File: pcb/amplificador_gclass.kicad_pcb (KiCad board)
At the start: 2 copper layers, 72 parts, among them P1 CONN_01X02, P2 CONN_01X02, P3 CONN_01X02, P4 CONN_01X02, P5 BNC, P6 BNC, Q1 Q_PNP_EBC, Q10 Q_NPN_EBC, Q11 Q_PNP_EBC, Q12 Q_NPN_EBC, Q13 Q_PNP_EBC, Q14 Q_NPN_ECB, Q15 Q_PNP_EBC, Q16 Q_NPN_ECB, Q17 Q_NPN_ECB, Q18 Q_PNP_EBC, Q19 Q_NPN_ECB, Q2 Q_PNP_EBC, Q20 Q_PNP_EBC, Q21 Q_NPN_ECB, Q22 Q_PNP_EBC, Q23 Q_NPN_ECB, Q24 Q_NPN_ECB, Q25 Q_PNP_EBC, Q26 Q_PNP_EBC, Q3 Q_NPN_EBC, Q4 Q_PNP_EBC, Q5 Q_NPN_EBC, Q6 Q_PNP_EBC, Q7 Q_PNP_EBC, Q8 Q_PNP_EBC, Q9 Q_PNP_EBC

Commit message: Agrego algunos datasheets, el export kicad en pdf y sigo trabajando en el PCB
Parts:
- removed Q21: Q_NPN_ECB, Transistors_TO-220:TO-220_Bipolar-BCE_Vertical_LargePads
- removed Q22: Q_PNP_EBC, Transistors_TO-220:TO-220_Bipolar-BCE_Vertical_LargePads
- removed Q23, Q24: Q_NPN_ECB, Transistors_TO-220:TO-220_Bipolar-BCE_Horizontal
- removed Q25, Q26: Q_PNP_EBC, Transistors_TO-220:TO-220_Bipolar-BCE_Horizontal
- added C7: C, Capacitors_SMD:C_0603_HandSoldering, F.Cu at (178.1, 52.2)
- added P10: 2SC3281, Pin_Headers:Pin_Header_Straight_1x03, F.Cu at (138.3, 121.8)
- added P11: 2SC3281, Pin_Headers:Pin_Header_Straight_1x03, F.Cu at (144.7, 108.5)
- added P12: 2SA1302, Pin_Headers:Pin_Header_Straight_1x03, F.Cu at (131.3, 108.5)
- added P7: MJE350, Pin_Headers:Pin_Header_Straight_1x03, F.Cu at (138.0, 108.5)
- added P8: MJE340, Pin_Headers:Pin_Header_Straight_1x03, F.Cu at (116.9, 130.5)
- added P9: 2SA1302, Pin_Headers:Pin_Header_Straight_1x03, F.Cu at (131.1, 121.8)
- Q1, Q11, Q13, Q15, Q2, Q4, Q6, Q7, Q8, Q9: value Q_PNP_EBC -> MPSA56_PNP_EBC; footprint Transistors_TO-220:TO-220_Bipolar-BCE_Vertical_LargePads -> Transistors_TO-220:TO-220_Neutral123_Vertical
- Q10, Q12, Q3, Q5: value Q_NPN_EBC -> MPSA06_NPN_EBC; footprint Transistors_TO-220:TO-220_Bipolar-BCE_Vertical_LargePads -> Transistors_TO-220:TO-220_Neutral123_Vertical
- Q14, Q16: value Q_NPN_ECB -> MPSA06_NPN_EBC; footprint Transistors_TO-220:TO-220_Bipolar-BCE_Vertical_LargePads -> Transistors_TO-220:TO-220_Neutral123_Vertical
- Q17, Q19: value Q_NPN_ECB -> MJE340_NPN_ECB; footprint Transistors_TO-220:TO-220_Bipolar-BCE_Vertical_LargePads -> Transistors_TO-220:TO-220_Neutral123_Vertical
- Q18, Q20: value Q_PNP_EBC -> MJE350_PNP_EBC; footprint Transistors_TO-220:TO-220_Bipolar-BCE_Vertical_LargePads -> Transistors_TO-220:TO-220_Neutral123_Vertical
- moved R24 204.7 mm to (136.0, 140.1)
- moved R15 195.0 mm to (118.2, 140.6)
- moved R20 194.5 mm to (131.5, 140.1)
- moved R28 192.5 mm to (113.3, 140.8)
- moved R25 189.7 mm to (146.7, 136.3)
- moved R22 188.1 mm to (146.7, 130.4)
- moved R26 187.1 mm to (140.4, 140.1)
- moved R17 185.1 mm to (127.1, 140.1)
- moved R16 185.1 mm to (122.6, 140.1)
- moved R23 184.0 mm to (153.1, 121.7)
- moved R21 177.0 mm to (148.6, 121.7)
- moved C3 176.7 mm to (116.1, 92.4)
- moved C5 175.8 mm to (151.0, 127.6)
- moved C1 174.9 mm to (116.1, 86.5)
- moved R12 174.0 mm to (145.4, 96.0)
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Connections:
- C4 pad 2: (no net) -> Net-(C4-Pad2)
- C5 pad 2: TO_OPS -> Net-(C5-Pad2)
- C6 pad 1: Net-(C6-Pad1) -> (no net)
- C6 pad 2: TO_OPS -> -VA
- D2 pad 1: Net-(C6-Pad1) -> Net-(C5-Pad2)
- D3 pad 1: (no net) -> Net-(D3-Pad1)
- D4 pad 2: (no net) -> Net-(D4-Pad2)
- P1 pad 1: (no net) -> +VA
- R12 pad 1: (no net) -> Net-(Q11-Pad2)
- R13 pad 1: (no net) -> Net-(Q10-Pad1)
- R14 pad 1: (no net) -> Net-(Q12-Pad1)
- R15 pad 1: (no net) -> Net-(Q13-Pad2)
- R16 pad 1: (no net) -> Net-(Q14-Pad2)
- R17 pad 1: (no net) -> Net-(Q17-Pad3)
- R18 pad 1: (no net) -> Net-(Q18-Pad2)
- R18 pad 2: Net-(C6-Pad1) -> Net-(C5-Pad2)
- R21 pad 2: Net-(C6-Pad1) -> Net-(C5-Pad2)
- R22 pad 2: (no net) -> Net-(P10-Pad1)
- R23 pad 2: (no net) -> Net-(P9-Pad1)
- R24 pad 2: (no net) -> Net-(P11-Pad1)
- R25 pad 2: (no net) -> Net-(P12-Pad1)
- R26 pad 2: (no net) -> Net-(P10-Pad3)
- R27 pad 2: (no net) -> Net-(P9-Pad3)
- R4 pad 2: (no net) -> Net-(Q1-Pad1)
- R5 pad 1: (no net) -> Net-(Q3-Pad1)
- R7 pad 2: (no net) -> Net-(Q7-Pad1)
- R8 pad 1: (no net) -> Net-(Q5-Pad1)
- R9 pad 1: (no net) -> Net-(Q4-Pad2)

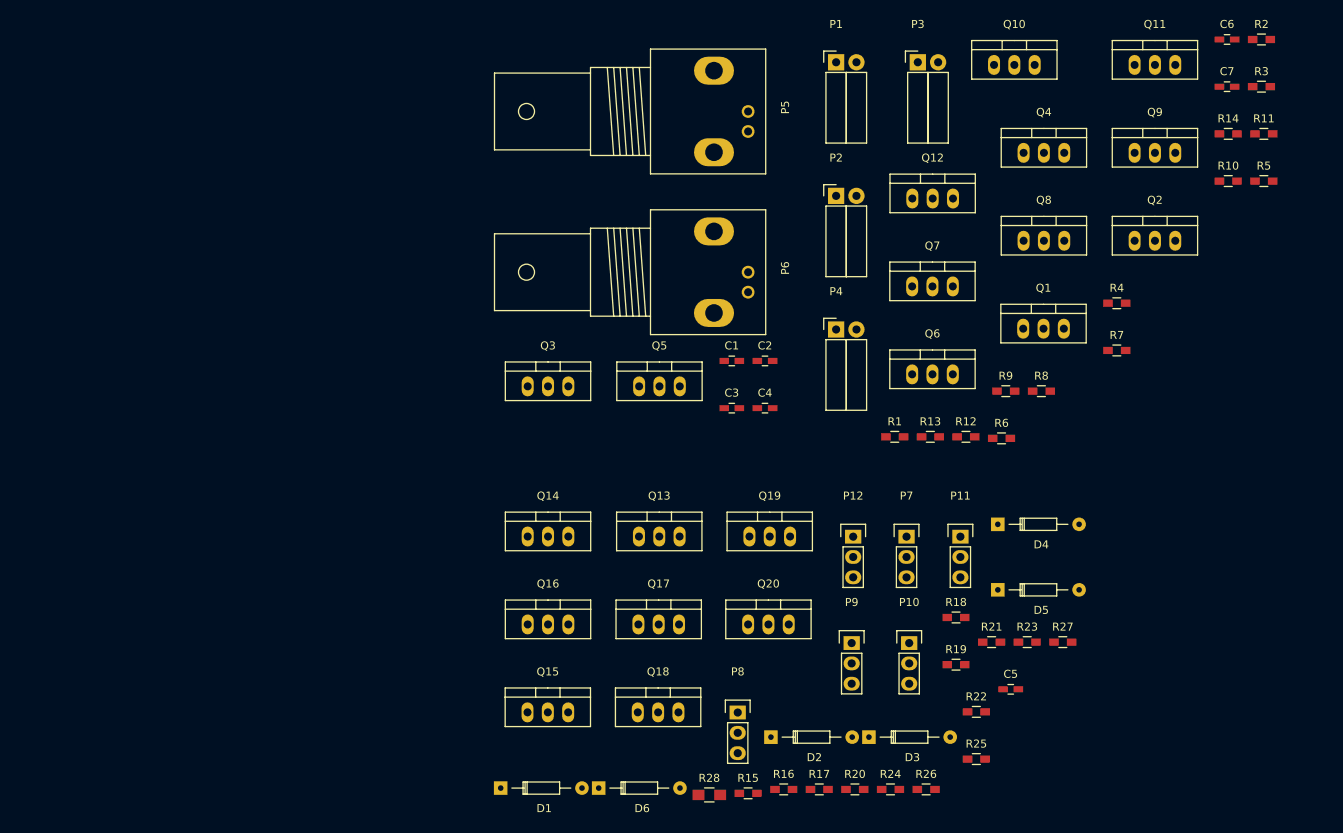
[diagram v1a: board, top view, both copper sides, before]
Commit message: Termino la primera version del PCB para el amplificador, queda engordar las pistas que llevan alta corriente.
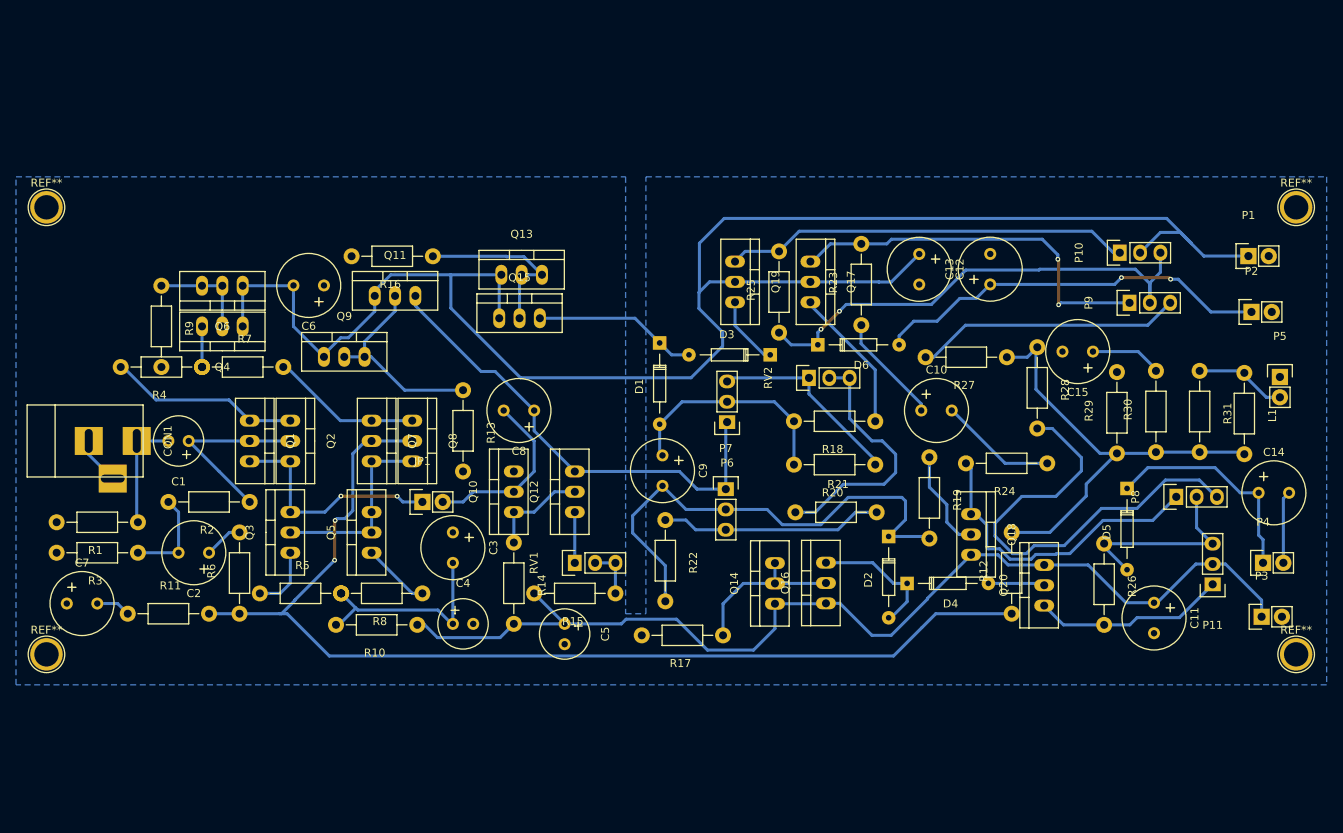
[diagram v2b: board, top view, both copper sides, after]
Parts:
- removed P12: 2SA1302, Pin_Headers:Pin_Header_Straight_1x03
- added C10: C, Capacitors_Elko_ThroughHole:Elko_vert_11.5x8mm_RM3.5, F.Cu at (139.8, 92.7)
- added C11: C, Capacitors_Elko_ThroughHole:Elko_vert_11.5x8mm_RM3.5, F.Cu at (168.9, 116.7)
- added C12: C, Capacitors_Elko_ThroughHole:Elko_vert_11.5x8mm_RM3.5, F.Cu at (139.6, 73.2)
- added C13: C, Capacitors_Elko_ThroughHole:Elko_vert_11.5x8mm_RM3.5, F.Cu at (148.4, 77.0)
- added C14: C, Capacitors_Elko_ThroughHole:Elko_vert_11.5x8mm_RM3.5, F.Cu at (182.0, 103.0)
- added C15: C, Capacitors_Elko_ThroughHole:Elko_vert_11.5x8mm_RM3.5, F.Cu at (161.3, 85.3)
- added C8: C, Capacitors_Elko_ThroughHole:Elko_vert_11.5x8mm_RM3.5, F.Cu at (91.4, 92.7)
- added C9: C, Capacitors_Elko_ThroughHole:Elko_vert_11.5x8mm_RM3.5, F.Cu at (107.5, 98.3)
- added CON1: AUDIO_IN, Connect:BARREL_JACK, F.Cu at (35.6, 96.5)
- added JP1: JUMPER, Socket_Strips:Socket_Strip_Straight_1x02, F.Cu at (77.5, 104.1)
- added L1: INDUCTOR, Resistors_ThroughHole:Resistor_Horizontal_RM10mm, F.Cu at (180.2, 93.1)
- added R29: R, Resistors_ThroughHole:Resistor_Horizontal_RM10mm, F.Cu at (164.3, 93.0)
- added R30: R, Resistors_ThroughHole:Resistor_Horizontal_RM10mm, F.Cu at (169.2, 92.8)
- added R31: R, Resistors_ThroughHole:Resistor_Horizontal_RM10mm, F.Cu at (174.6, 92.8)
- added REF**: 1pin, Connect:1pin, F.Cu at (186.7, 67.3)
- added REF**: 1pin, Connect:1pin, F.Cu at (186.7, 123.2)
- added REF**: 1pin, Connect:1pin, F.Cu at (30.5, 67.3)
- added REF**: 1pin, Connect:1pin, F.Cu at (30.5, 123.2)
- added RV1: POT, Pin_Headers:Pin_Header_Straight_1x03, F.Cu at (96.5, 111.8)
- added RV2: POT, Pin_Headers:Pin_Header_Straight_1x03, F.Cu at (125.8, 88.6)
- C1, C4, C5: footprint Capacitors_SMD:C_0603_HandSoldering -> Capacitors_Elko_ThroughHole:Elko_vert_11.2x6.3mm_RM2.5_CopperClear
- C2, C3, C6, C7: footprint Capacitors_SMD:C_0603_HandSoldering -> Capacitors_Elko_ThroughHole:Elko_vert_11.5x8mm_RM3.5
- D1: value D_Schottky -> ZENER
- P1: value CONN_01X02 -> +VA_GND; footprint Socket_Strips:Socket_Strip_Angled_1x02 -> Socket_Strips:Socket_Strip_Straight_1x02
- P11: value 2SC3281 -> 2SA1302
- P2: value CONN_01X02 -> +VB_GND; footprint Socket_Strips:Socket_Strip_Angled_1x02 -> Socket_Strips:Socket_Strip_Straight_1x02
- P3: value CONN_01X02 -> -VA_GND; footprint Socket_Strips:Socket_Strip_Angled_1x02 -> Socket_Strips:Socket_Strip_Straight_1x02
- P4: value CONN_01X02 -> -VB_GND; footprint Socket_Strips:Socket_Strip_Angled_1x02 -> Socket_Strips:Socket_Strip_Straight_1x02
- P5: value BNC -> OUT; footprint Sockets_BNC:BNC_Socket_TYCO-AMP -> Pin_Headers:Pin_Header_Straight_1x02
- P6: value BNC -> MJE350; footprint Sockets_BNC:BNC_Socket_TYCO-AMP -> Pin_Headers:Pin_Header_Straight_1x03
- P7: value MJE350 -> MJE340
- P8: value MJE340 -> 2SA1302
- P9: value 2SA1302 -> 2SC3281
- R1, R10, R11, R12, R13, R14, R15, R16, R17, R18, R19, R2, R20, R21, R22, R23, R24, R25, R26, R27, R3, R4, R5, R6, R7, R8, R9: footprint Resistors_SMD:R_0603_HandSoldering -> Resistors_ThroughHole:Resistor_Horizontal_RM10mm
- R28: footprint Resistors_SMD:R_0805_HandSoldering -> Resistors_ThroughHole:Resistor_Horizontal_RM10mm
- moved C7 158.8 mm to (33.0, 116.8)
- moved R3 156.8 mm to (36.8, 110.5), turned to 180 degrees
- moved R11 149.5 mm to (45.7, 118.1)
- moved R2 143.7 mm to (50.8, 104.1), turned to 180 degrees
- moved R5 131.0 mm to (62.2, 115.6)
- moved R10 120.0 mm to (71.8, 119.5), turned to 180 degrees
- moved R4 119.7 mm to (44.8, 87.3), turned to 180 degrees
- moved C6 117.0 mm to (65.2, 77.1), turned to 180 degrees
- moved Q2 110.9 mm to (61.0, 96.5), turned to 270 degrees
- moved R7 109.3 mm to (55.0, 87.3)
- moved R9 105.9 mm to (44.8, 82.2), turned to 270 degrees
- moved R14 105.5 mm to (88.9, 114.3), turned to 270 degrees
- moved Q4 105.0 mm to (52.5, 82.2), turned to 180 degrees
- moved Q9 104.5 mm to (67.7, 86.0)
- moved R1 100.3 mm to (36.8, 106.7), turned to 180 degrees
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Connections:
- C3 pad 1: GND -> (no net)
- C4 pad 1: TO_OPS -> Net-(C3-Pad2)
- C4 pad 2: Net-(C4-Pad2) -> GND
- C5 pad 1: Net-(C5-Pad1) -> -VA
- C5 pad 2: Net-(C5-Pad2) -> GND
- C6 pad 1: (no net) -> GND
- C6 pad 2: -VA -> +VA
- C7 pad 1: (no net) -> GND
- C7 pad 2: (no net) -> Net-(C7-Pad2)
- D1 pad 2: Net-(C5-Pad1) -> Net-(C9-Pad1)
- D2 pad 1: Net-(C5-Pad2) -> Net-(C9-Pad2)
- D5 pad 1: Net-(D5-Pad1) -> -VB
- D5 pad 2: +VB -> Net-(D5-Pad2)
- D6 pad 1: -VB -> Net-(D6-Pad1)
- D6 pad 2: Net-(D6-Pad2) -> +VB
- P10 pad 2: Net-(D5-Pad1) -> +VA
- P10 pad 3: Net-(P10-Pad3) -> Net-(D6-Pad1)
- P11 pad 2: +VA -> -VA
- P11 pad 3: Net-(D5-Pad1) -> Net-(D5-Pad2)
- P5 pad 1: IN -> GND
- P5 pad 2: GND -> OUT
- P6 pad 1: OUT -> TO_OPS
- P6 pad 2: GND -> Net-(C9-Pad1)
- P7 pad 2: Net-(C5-Pad1) -> Net-(C9-Pad2)
- P8 pad 1: TO_OPS -> Net-(P8-Pad1)
- P8 pad 2: Net-(C5-Pad2) -> Net-(D5-Pad2)
- P9 pad 2: Net-(D6-Pad2) -> Net-(D6-Pad1)
- Q10 pad 2: Net-(C4-Pad2) -> Net-(C8-Pad2)
- Q17 pad 1: Net-(P10-Pad1) -> Net-(P9-Pad1)
- Q18 pad 1: Net-(P9-Pad1) -> Net-(P8-Pad1)
- Q19 pad 1: Net-(P11-Pad1) -> Net-(P10-Pad1)
- Q20 pad 1: Net-(P12-Pad1) -> Net-(P11-Pad1)
- R10 pad 1: Net-(C3-Pad2) -> -VA
- R10 pad 2: Net-(Q7-Pad2) -> Net-(C3-Pad2)
- R11 pad 1: Net-(Q7-Pad2) -> Net-(C7-Pad2)
- R11 pad 2: OUT -> Net-(Q7-Pad2)
- R12 pad 1: Net-(Q11-Pad2) -> Net-(Q7-Pad2)
- R12 pad 2: GND -> FBACK
- R13 pad 1: Net-(Q10-Pad1) -> Net-(Q11-Pad2)
- R13 pad 2: -VA -> GND
- R14 pad 1: Net-(Q12-Pad1) -> Net-(Q10-Pad1)
- R15 pad 1: Net-(Q13-Pad2) -> Net-(R15-Pad1)
- R15 pad 2: GND -> -VA
- R16 pad 1: Net-(Q14-Pad2) -> Net-(Q13-Pad2)
- R17 pad 1: Net-(Q17-Pad3) -> Net-(Q14-Pad2)
- R17 pad 2: Net-(C5-Pad1) -> GND
- R18 pad 1: Net-(Q18-Pad2) -> Net-(Q17-Pad3)
- R18 pad 2: Net-(C5-Pad2) -> Net-(C9-Pad1)
- R19 pad 1: Net-(P7-Pad3) -> Net-(Q18-Pad2)
- R19 pad 2: Net-(C5-Pad1) -> Net-(C9-Pad2)
- R20 pad 1: Net-(P8-Pad3) -> Net-(P6-Pad3)
- R20 pad 2: Net-(P7-Pad3) -> Net-(C9-Pad1)
- R21 pad 1: Net-(P8-Pad3) -> Net-(R21-Pad1)
- R21 pad 2: Net-(C5-Pad2) -> Net-(P7-Pad3)
- R22 pad 1: Net-(R22-Pad1) -> Net-(P7-Pad3)
- R22 pad 2: Net-(P10-Pad1) -> Net-(C9-Pad2)
- R23 pad 1: Net-(R22-Pad1) -> Net-(C10-Pad1)
- R24 pad 1: Net-(D5-Pad1) -> Net-(C10-Pad2)
- R24 pad 2: Net-(P11-Pad1) -> Net-(P8-Pad1)
- R25 pad 1: Net-(D6-Pad2) -> Net-(D6-Pad1)
- R25 pad 2: Net-(P12-Pad1) -> Net-(P10-Pad1)
- R26 pad 1: OUT -> Net-(D5-Pad2)
- R26 pad 2: Net-(P10-Pad3) -> Net-(P11-Pad1)
- R27 pad 1: OUT -> FBACK
- R28 pad 1: OUT -> FBACK
- R28 pad 2: GND -> Net-(P8-Pad3)
- R5 pad 2: -VA -> Net-(C3-Pad2)
- R8 pad 2: -VA -> Net-(C3-Pad2)
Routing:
- net +VA: track 0.00 -> 222.4 mm
- net Net-(Q7-Pad2): track 0.00 -> 137.3 mm, vias 0 -> 2
- net -VA: track 0.00 -> 132.7 mm
- net Net-(C9-Pad2): track 0.00 -> 62.2 mm
- net Net-(D6-Pad1): track 0.00 -> 61.8 mm, vias 0 -> 2
- net TO_OPS: track 0.00 -> 59.5 mm
- net FBACK: track 0.00 -> 57.8 mm
- net Net-(P8-Pad3): track 0.00 -> 57.5 mm
- net Net-(P10-Pad1): track 0.00 -> 50.8 mm
- net +VB: track 0.00 -> 49.9 mm, vias 0 -> 2
- net Net-(P9-Pad1): track 0.00 -> 48.2 mm, vias 0 -> 2
- net Net-(P8-Pad1): track 0.00 -> 39.5 mm
- net Net-(P9-Pad3): track 0.00 -> 33.4 mm
- net Net-(R21-Pad1): track 0.00 -> 32.1 mm
- net Net-(JP1-Pad1): track 0.00 -> 29.1 mm, vias 0 -> 2
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- added copper zone on B.Cu, net GND
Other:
- net class Default: clearance 0.2 -> 0.254; trace_width 0.25 -> 0.381
- rule trace_clearance: 0.2 -> 0.254
- rule trace_min: 0.2 -> 0.2286
- rule via_min_size: 0.4 -> 0.508

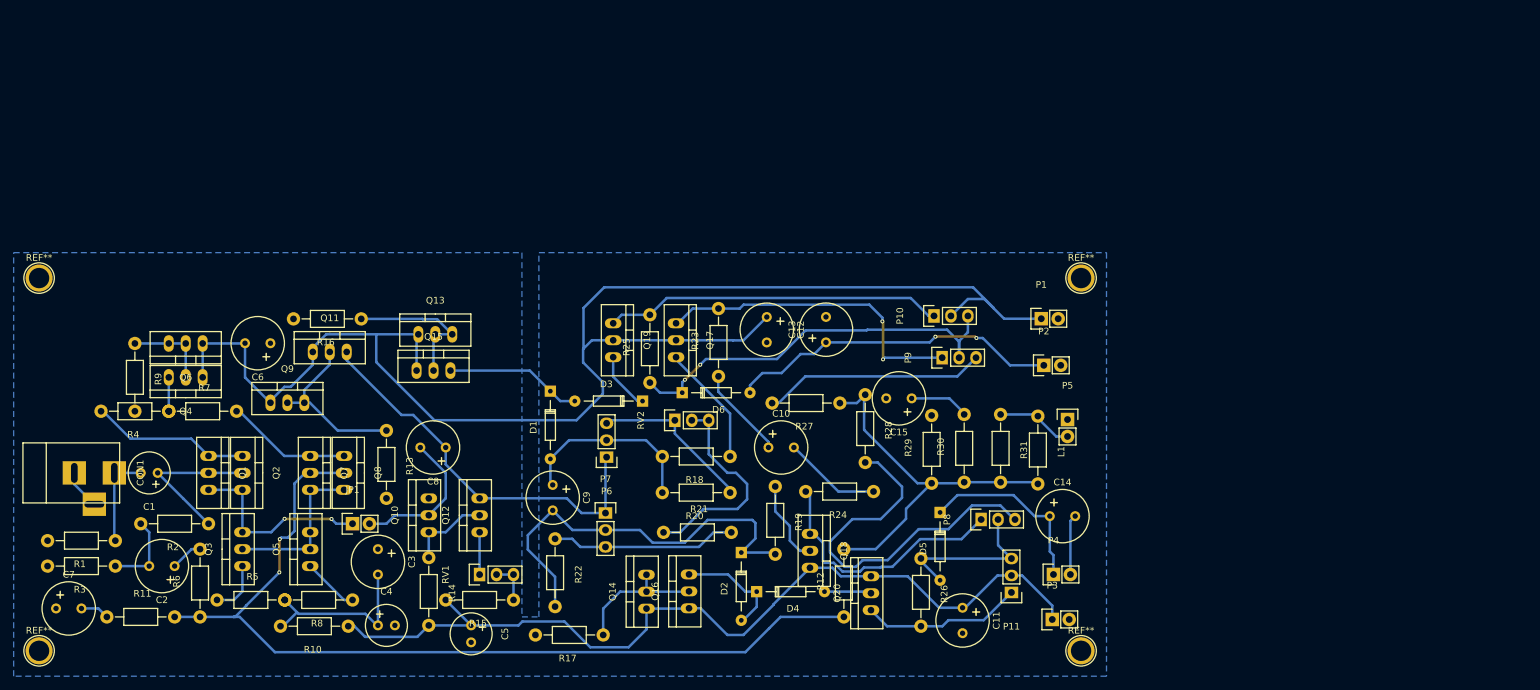
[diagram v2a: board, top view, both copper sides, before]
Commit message: Arreglo problema, se mostraba cobre en el front , solo lo hice para Q1, queda hacerlo en todos y ajustar bien los drills, acorde a los que existen en el LCI...
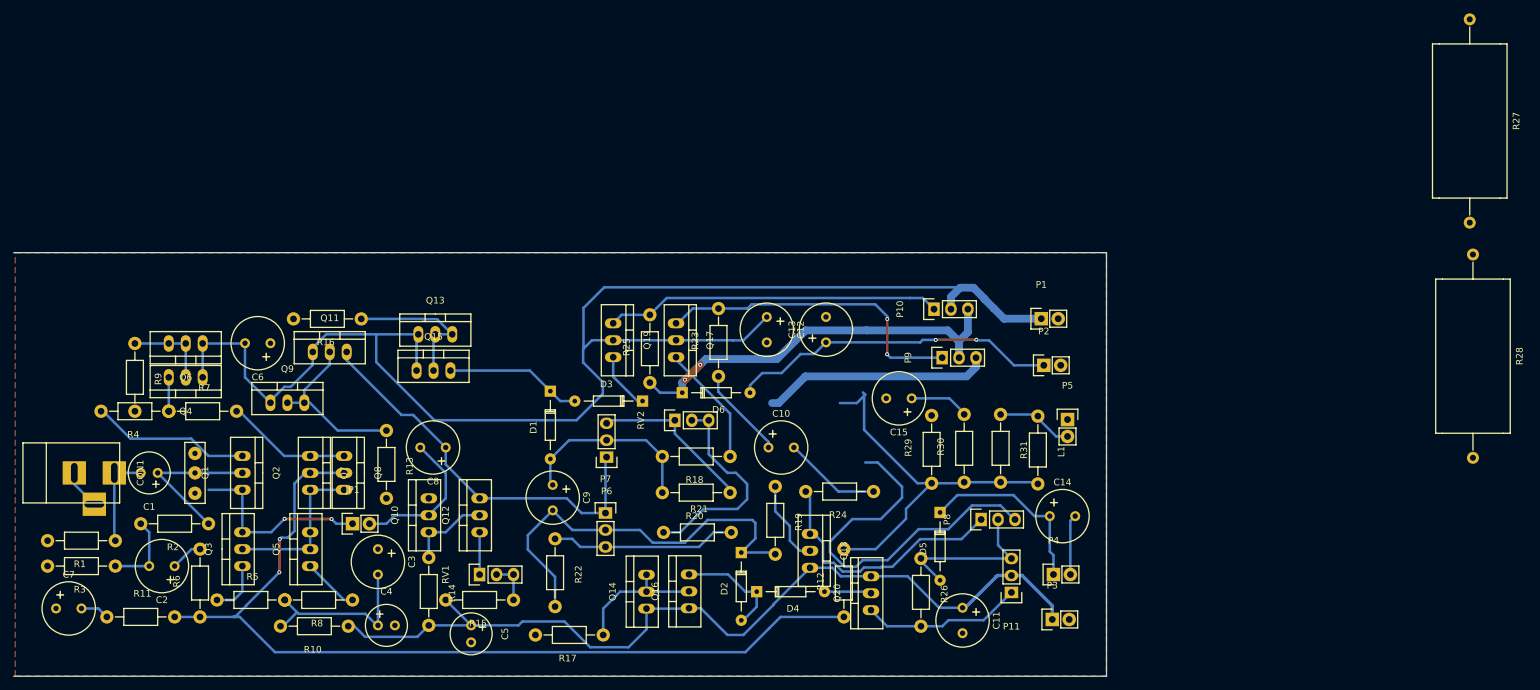
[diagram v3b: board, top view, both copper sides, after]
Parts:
- removed REF** (x4): 1pin, Connect:1pin
- Q1: footprint Transistors_TO-220:TO-220_Neutral123_Vertical -> pcb:TRANSISTOR_PARA_GCLASS
- R27, R28: footprint Resistors_ThroughHole:Resistor_Horizontal_RM10mm -> Resistors_ThroughHole:Resistor_Ceramic_Horizontal_L23mm-W9mm-H9mm-p30mm
- moved R27 108.1 mm to (245.0, 43.8), turned to 270 degrees
- moved R28 91.8 mm to (245.4, 79.0)
- moved P10 1.02 mm to (164.6, 72.0)
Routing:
- net -VA: track 132.7 -> 149.8 mm
- net Net-(P9-Pad3): track 33.4 -> 40.8 mm
- net Net-(D6-Pad1): track 61.8 -> 66.0 mm
- net +VA: track 222.4 -> 224.5 mm
- added copper zone on F.Cu, net GND
- removed copper zone on B.Cu, net GND
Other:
- board outline added: 163.8 x 63.5 mm
- net class Default: trace_width 0.381 -> 1.1684

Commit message: Cambio footprints, empiezo a re-rutear
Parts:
- removed JP1: JUMPER, Socket_Strips:Socket_Strip_Straight_1x02
- added P12: 2SA1302, pcb:bornera_grande, F.Cu at (226.2, 121.3)
- P10: footprint Pin_Headers:Pin_Header_Straight_1x03 -> pcb:bornera_grande
- P11: value 2SA1302 -> 2SC3281; footprint Pin_Headers:Pin_Header_Straight_1x03 -> pcb:bornera_grande
- P6: value MJE350 -> CONN_01X01
- P7: value MJE340 -> MJE350
- P8: value 2SA1302 -> MJE340
- P9: value 2SC3281 -> 2SA1302; footprint Pin_Headers:Pin_Header_Straight_1x03 -> pcb:bornera_grande
- Q1: footprint pcb:TRANSISTOR_PARA_GCLASS -> pcb:MPSA06-56_TO92_EBC
- Q10, Q11, Q12, Q13, Q14, Q15, Q16, Q2, Q3, Q4, Q5, Q6, Q7, Q8, Q9: footprint Transistors_TO-220:TO-220_Neutral123_Vertical -> pcb:MPSA06-56_TO92_EBC
- Q19: footprint Transistors_TO-220:TO-220_Neutral123_Vertical -> pcb:MJE340_gclass
- Q20: footprint Transistors_TO-220:TO-220_Neutral123_Vertical -> pcb:MJE_350_gclass
- R27, R28: footprint Resistors_ThroughHole:Resistor_Ceramic_Horizontal_L23mm-W9mm-H9mm-p30mm -> pcb:RESIST_35MMX10MM
- moved P10 59.5 mm to (217.9, 45.3)
- moved P11 58.3 mm to (234.3, 109.3)
- moved P9 56.0 mm to (221.9, 79.2)
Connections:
- P10 pad 2: +VA -> Net-(D6-Pad1)
- P10 pad 3: Net-(D6-Pad1) -> Net-(P10-Pad3)
- P11 pad 2: -VA -> +VA
- P11 pad 3: Net-(D5-Pad2) -> Net-(D6-Pad1)
- P6 pad 1: TO_OPS -> Net-(C8-Pad2)
- P6 pad 2: Net-(C9-Pad1) -> (no net)
- P6 pad 3: Net-(P6-Pad3) -> (no net)
- P7 pad 2: Net-(C9-Pad2) -> Net-(C9-Pad1)
- P8 pad 1: Net-(P8-Pad1) -> TO_OPS
- P8 pad 2: Net-(D5-Pad2) -> Net-(C9-Pad2)
- P9 pad 2: Net-(D6-Pad1) -> Net-(D5-Pad2)
- Q1 pad 3: Net-(JP1-Pad1) -> Net-(C8-Pad2)
- Q17 pad 1: Net-(P9-Pad1) -> Net-(P10-Pad1)
- Q18 pad 1: Net-(P8-Pad1) -> Net-(P9-Pad1)
- Q19 pad 1: Net-(P10-Pad1) -> Net-(P11-Pad1)
- Q2 pad 3: Net-(JP1-Pad1) -> Net-(C8-Pad2)
- Q20 pad 1: Net-(P11-Pad1) -> Net-(P12-Pad1)
- Q3 pad 3: Net-(JP1-Pad1) -> Net-(C8-Pad2)
- R20 pad 1: Net-(P6-Pad3) -> Net-(P7-Pad3)
- R21 pad 2: Net-(P7-Pad3) -> Net-(P8-Pad3)
- R22 pad 1: Net-(P7-Pad3) -> Net-(P8-Pad3)
- R23 pad 2: Net-(P9-Pad1) -> Net-(P10-Pad1)
- R24 pad 2: Net-(P8-Pad1) -> Net-(P9-Pad1)
- R25 pad 2: Net-(P10-Pad1) -> Net-(P11-Pad1)
- R26 pad 2: Net-(P11-Pad1) -> Net-(P12-Pad1)
- R27 pad 2: Net-(P9-Pad3) -> Net-(P10-Pad3)
- R28 pad 2: Net-(P8-Pad3) -> Net-(P9-Pad3)
- RV2 pad 1: Net-(P6-Pad3) -> Net-(P7-Pad3)
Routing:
- net (no net): track 0.00 -> 94.1 mm, vias 0 -> 2
- net Net-(P9-Pad3): track 40.8 -> 0.00 mm
- net Net-(P8-Pad1): track 39.5 -> 0.00 mm
- net Net-(P9-Pad1): track 47.8 -> 9.12 mm, vias 2 -> 0
- net TO_OPS: track 59.5 -> 89.6 mm
- net Net-(JP1-Pad1): track 29.1 -> 0.00 mm, vias 2 -> 0
- net Net-(Q7-Pad2): track 137.3 -> 109.8 mm, vias 2 -> 0
- net Net-(P11-Pad1): track 24.2 -> 50.4 mm
- net Net-(P6-Pad3): track 24.7 -> 0.00 mm
- net Net-(P12-Pad1): track 0.00 -> 24.2 mm
- net Net-(Q3-Pad2): track 24.1 -> 0.00 mm
- net Net-(P7-Pad3): track 27.8 -> 47.3 mm
- net GND: track 15.0 -> 31.8 mm
- net Net-(C8-Pad2): track 22.2 -> 5.62 mm
- net Net-(C9-Pad1): track 28.4 -> 38.6 mm
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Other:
- net class Default: trace_width 1.1684 -> 0.381
